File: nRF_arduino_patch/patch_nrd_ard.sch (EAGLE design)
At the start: 14 parts

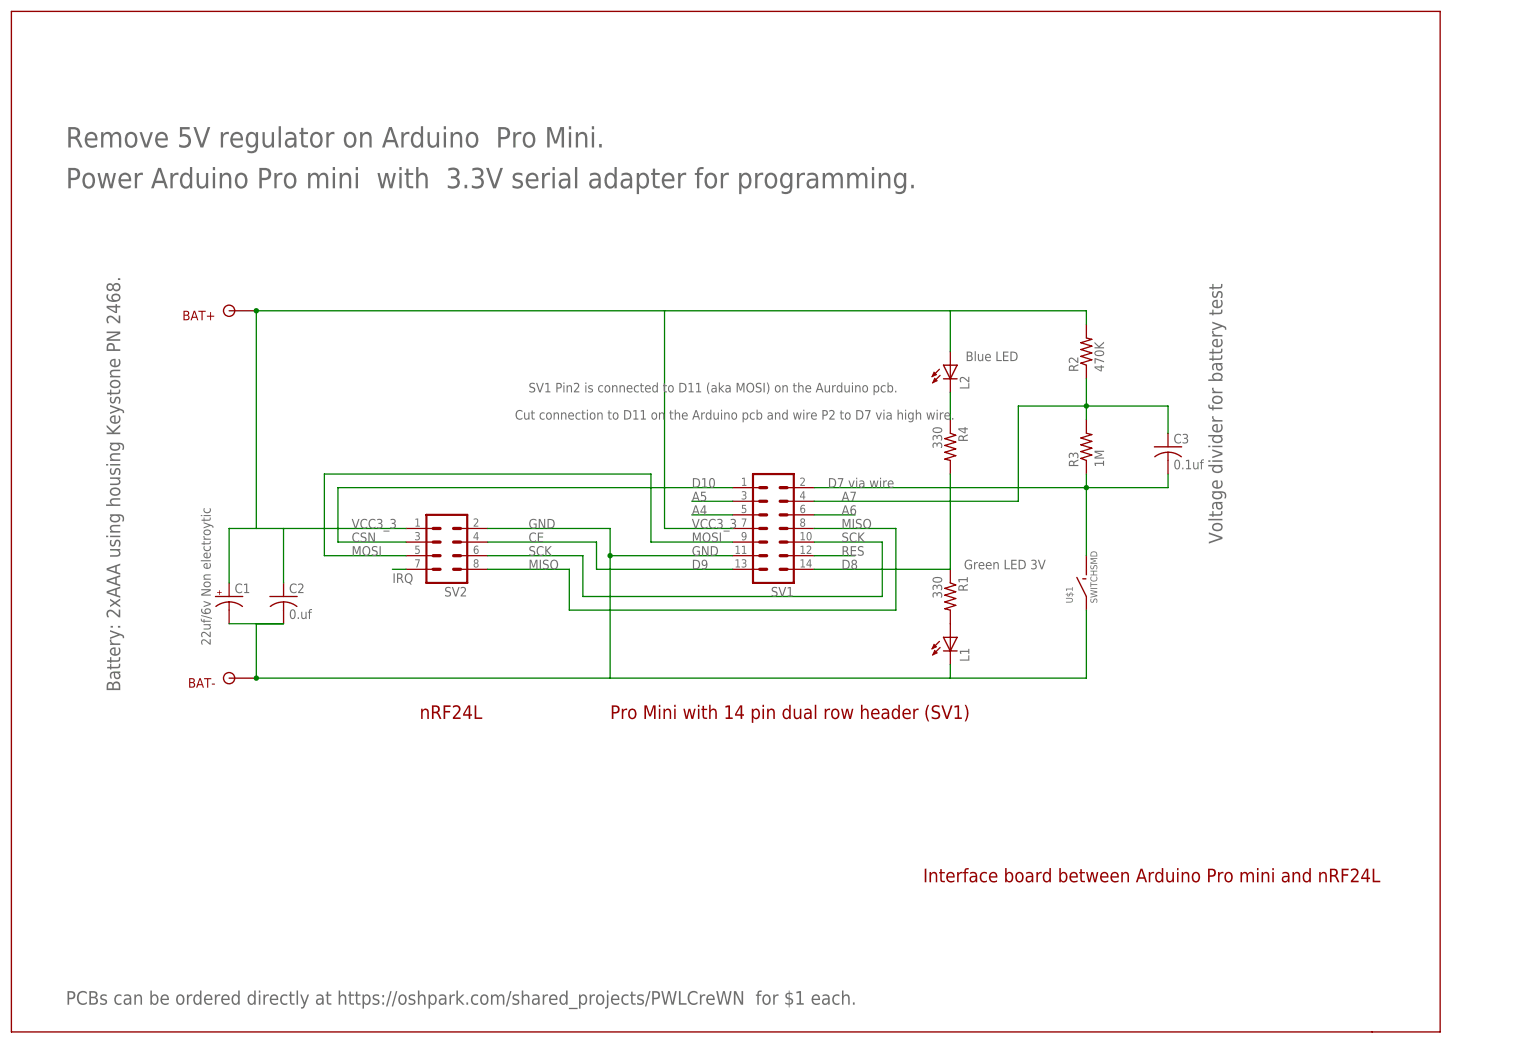
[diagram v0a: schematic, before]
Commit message: added  Nano Modem some modifications on nRFPatch board
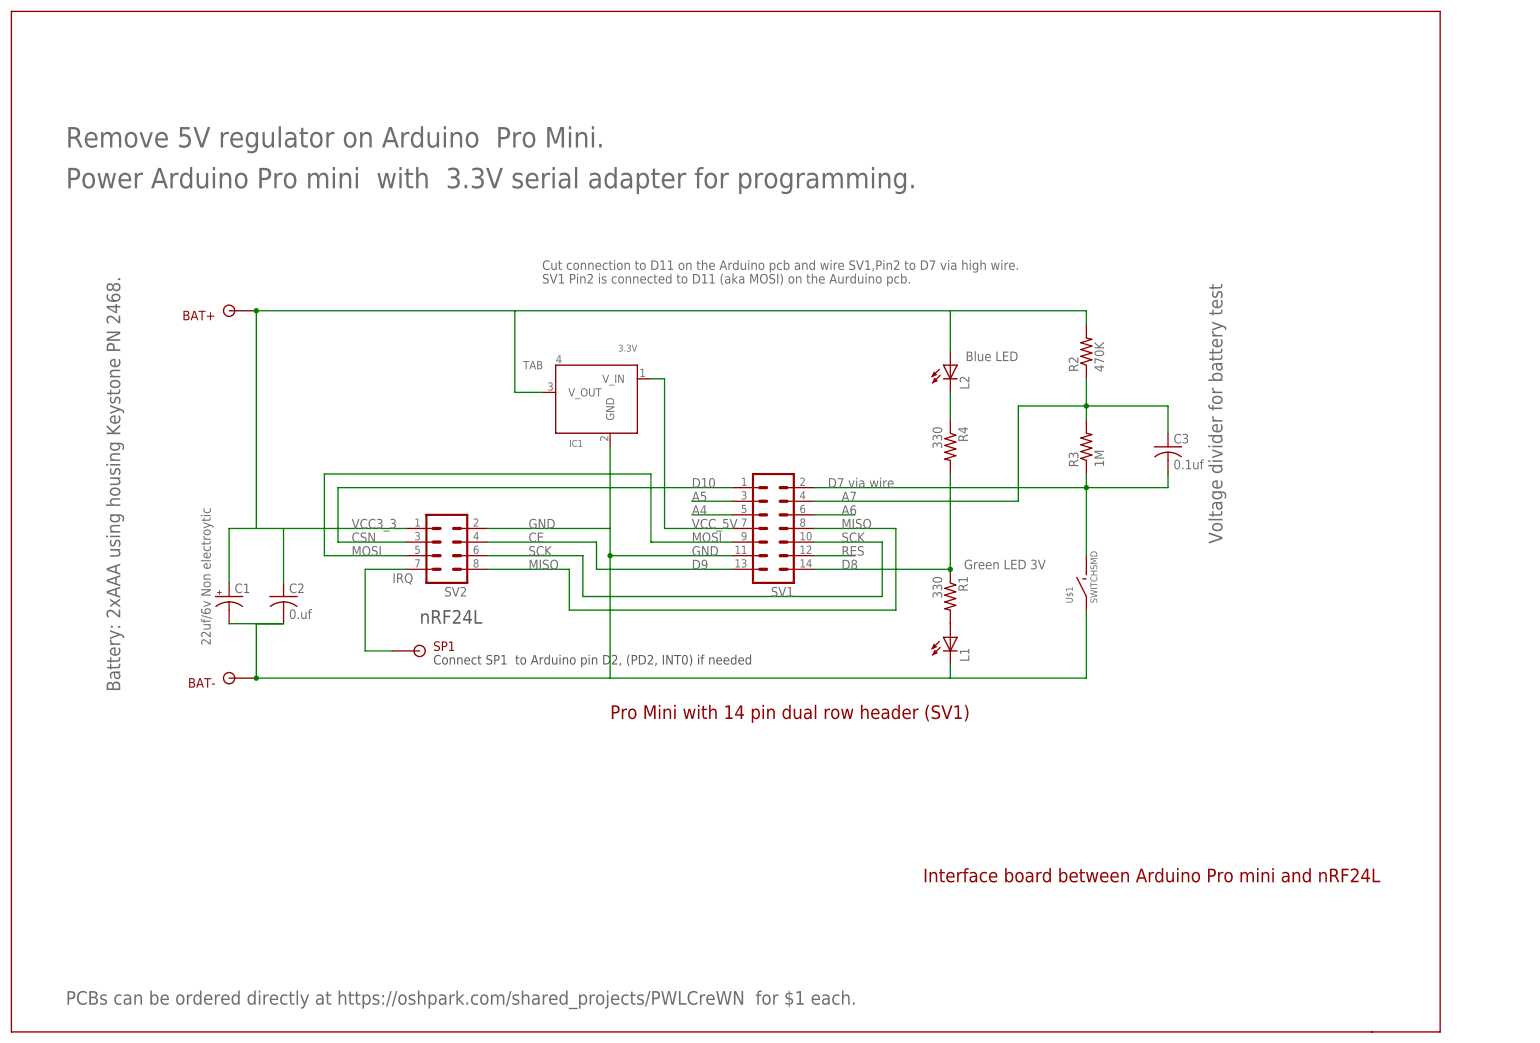
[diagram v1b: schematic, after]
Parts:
- added IC1: 3.3V, 1AA_Stofer:MCP1703ASOT223
- added SP1: SOLDER_POINTA, 1AA_Stofer:SOLDER_POINTA
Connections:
- new net VCC_5V: IC1.V_IN, SV1.7
- net GND: now also IC1.GND
- net IRQ: now also SP1.P$1
- net VCC3_3: now also IC1.V_OUT; no longer SV1.7
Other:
- note added: "Connect SP1 to Arduino pin D2, (PD2, INT0) if needed"
- note added: "Cut connection to D11 on the Arduino pcb and wire SV1,Pin2 to D7 via high wire."
- note removed: "Cut connection to D11 on the Arduino pcb and wire P2 to D7 via high wire."
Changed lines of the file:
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@@
 <layer number="106" name="BGA-Top" color="4" fill="1" visible="yes" active="yes"/>
 <layer number="107" name="BD-Top" color="5" fill="1" visible="yes" active="yes"/>
+<layer number="108" name="centerline" color="7" fill="1" visible="yes" active="yes"/>
 <layer number="116" name="Patch_BOT" color="9" fill="4" visible="yes" active="yes"/>
 <layer number="121" name="_tsilk" color="7" fill="1" visible="yes" active="yes"/>
 <layer number="122" name="_bsilk" color="7" fill="1" visible="yes" active="yes"/>
 <layer number="125" name="_tNames" color="7" fill="1" visible="yes" active="yes"/>
+<layer number="131" name="prix" color="7" fill="1" visible="yes" active="yes"/>
+<layer number="132" name="test" color="7" fill="1" visible="yes" active="yes"/>
 <layer number="144" name="Drill_legend" color="7" fill="1" visible="yes" active="yes"/>
 <layer number="151" name="HeatSink" color="7" fill="1" visible="yes" active="yes"/>
@@
 <part name="C3" library="rcl" deviceset="C-US" device="C0805" value="0.1uf"/>
 <part name="U$2" library="1AA_Stofer" deviceset="8.5X11" device=""/>
+<part name="IC1" library="1AA_Stofer" deviceset="MCP1703A" device="SOT223" value=" 3.3V"/>
+<part name="SP1" library="1AA_Stofer" deviceset="SOLDER_POINT" device="A"/>
 </parts>
 <sheets>
@@
 <text x="172.72" y="-25.4" size="2.54" layer="94">Interface board between Arduino Pro mini and nRF24L</text>
 <text x="114.3" y="5.08" size="2.54" layer="94">Pro Mini with 14 pin dual row header (SV1) </text>
-<text x="78.74" y="5.08" size="2.54" layer="94">nRF24L</text>
+<text x="78.74" y="22.86" size="2.54" layer="97">nRF24L</text>
 <text x="226.06" y="86.36" size="2.54" layer="95" rot="R270">Voltage divider for battery test</text>
 <text x="22.86" y="10.16" size="2.54" layer="95" rot="R90">Battery: 2xAAA using housing Keystone PN 2468. </text>
 <text x="190.5" y="73.66" size="1.778" layer="95" rot="R180">Blue LED </text>
 <text x="180.34" y="33.02" size="1.778" layer="95">Green LED 3V</text>
-<text x="96.52" y="60.96" size="1.778" layer="95">Cut connection to D11 on the Arduino pcb and wire P2 to D7 via high wire.</text>
-<text x="99.06" y="66.04" size="1.778" layer="95">SV1 Pin2 is connected to D11 (aka MOSI) on the Aurduino pcb. </text>
+<text x="101.6" y="88.9" size="1.778" layer="95">Cut connection to D11 on the Arduino pcb and wire SV1,Pin2 to D7 via high wire.</text>
+<text x="101.6" y="86.36" size="1.778" layer="95">SV1 Pin2 is connected to D11 (aka MOSI) on the Aurduino pcb. </text>
 <text x="12.7" y="-48.26" size="2.54" layer="95">PCBs can be ordered directly at https://oshpark.com/shared_projects/PWLCreWN  for $1 each.</text>
 <text x="12.7" y="111.76" size="3.81" layer="95">Remove 5V regulator on Arduino  Pro Mini.</text>
 <text x="12.7" y="104.14" size="3.81" layer="95">Power Arduino Pro mini  with  3.3V serial adapter for programming.</text>
+<text x="81.28" y="15.24" size="1.778" layer="97">Connect SP1  to Arduino pin D2, (PD2, INT0) if needed </text>
 </plain>
 <instances>
@@
 <instance part="U$2" gate="G$1" x="2.54" y="-53.34"/>
 <instance part="U$2" gate="G$2" x="167.64" y="-53.34"/>
+<instance part="IC1" gate="G$1" x="111.76" y="66.04" rot="MR0"/>
+<instance part="SP1" gate="G$1" x="83.82" y="17.78"/>
 </instances>
 <busses>
@@
 <pinref part="R4" gate="G$1" pin="2"/>
 <wire x1="177.8" y1="50.8" x2="177.8" y2="33.02" width="0.1524" layer="91"/>
+<junction x="177.8" y="33.02"/>
 </segment>
 </net>
@@
 <segment>
 <pinref part="SV2" gate="G$1" pin="7"/>
-<wire x1="76.2" y1="33.02" x2="73.66" y2="33.02" width="0.1524" layer="91"/>
 <label x="73.66" y="30.48" size="1.778" layer="95"/>
+<wire x1="76.2" y1="33.02" x2="68.58" y2="33.02" width="0.1524" layer="91"/>
+<wire x1="68.58" y1="33.02" x2="68.58" y2="17.78" width="0.1524" layer="91"/>
+<pinref part="SP1" gate="G$1" pin="P$1"/>
+<wire x1="68.58" y1="17.78" x2="73.66" y2="17.78" width="0.1524" layer="91"/>
 </segment>
 </net>
@@
 <net name="GND" class="0">
 <segment>
-<label x="129.54" y="35.56" size="1.778" layer="95"/>
 <pinref part="SV2" gate="G$1" pin="2"/>
 <label x="99.06" y="40.64" size="1.778" layer="95"/>
 <wire x1="91.44" y1="40.64" x2="114.3" y2="40.64" width="0.1524" layer="91"/>
-<wire x1="114.3" y1="40.64" x2="114.3" y2="35.56" width="0.1524" layer="91"/>
 <pinref part="C1" gate="G$1" pin="-"/>
 <wire x1="53.34" y1="22.86" x2="48.26" y2="22.86" width="0.1524" layer="91"/>
@@
 <pinref part="C2" gate="G$1" pin="2"/>
 <wire x1="43.18" y1="22.86" x2="53.34" y2="22.86" width="0.1524" layer="91"/>
+<wire x1="114.3" y1="40.64" x2="114.3" y2="35.56" width="0.1524" layer="91"/>
+<pinref part="L1" gate="G$1" pin="C"/>
 <wire x1="114.3" y1="35.56" x2="114.3" y2="12.7" width="0.1524" layer="91"/>
-<pinref part="L1" gate="G$1" pin="C"/>
 <wire x1="177.8" y1="15.24" x2="177.8" y2="12.7" width="0.1524" layer="91"/>
 <wire x1="48.26" y1="12.7" x2="114.3" y2="12.7" width="0.1524" layer="91"/>
 <wire x1="114.3" y1="12.7" x2="177.8" y2="12.7" width="0.1524" layer="91"/>
 <wire x1="203.2" y1="12.7" x2="177.8" y2="12.7" width="0.1524" layer="91"/>
-<junction x="114.3" y="35.56"/>
 <pinref part="U$1" gate="G$1" pin="P$2"/>
 <wire x1="203.2" y1="12.7" x2="203.2" y2="25.4" width="0.1524" layer="91"/>
+<pinref part="BAT-" gate="G$1" pin="P$1"/>
+<junction x="48.26" y="12.7"/>
+<pinref part="IC1" gate="G$1" pin="GND"/>
+<wire x1="114.3" y1="40.64" x2="114.3" y2="55.88" width="0.1524" layer="91"/>
 <pinref part="SV1" gate="G$1" pin="11"/>
 <wire x1="137.16" y1="35.56" x2="114.3" y2="35.56" width="0.1524" layer="91"/>
-<pinref part="BAT-" gate="G$1" pin="P$1"/>
-<junction x="48.26" y="12.7"/>
+<label x="129.54" y="35.56" size="1.778" layer="95"/>
+<junction x="114.3" y="35.56"/>
 </segment>
 </net>
@@
 <wire x1="43.18" y1="40.64" x2="48.26" y2="40.64" width="0.1524" layer="91"/>
 <wire x1="48.26" y1="40.64" x2="48.26" y2="81.28" width="0.1524" layer="91"/>
-<pinref part="SV1" gate="G$1" pin="7"/>
-<label x="129.54" y="40.64" size="1.778" layer="95"/>
-<wire x1="137.16" y1="40.64" x2="124.46" y2="40.64" width="0.1524" layer="91"/>
-<wire x1="124.46" y1="40.64" x2="124.46" y2="81.28" width="0.1524" layer="91"/>
-<wire x1="48.26" y1="81.28" x2="124.46" y2="81.28" width="0.1524" layer="91"/>
+<wire x1="48.26" y1="81.28" x2="96.52" y2="81.28" width="0.1524" layer="91"/>
 <pinref part="R2" gate="G$1" pin="2"/>
-<wire x1="124.46" y1="81.28" x2="177.8" y2="81.28" width="0.1524" layer="91"/>
+<wire x1="96.52" y1="81.28" x2="177.8" y2="81.28" width="0.1524" layer="91"/>
 <wire x1="177.8" y1="81.28" x2="203.2" y2="81.28" width="0.1524" layer="91"/>
 <wire x1="203.2" y1="81.28" x2="203.2" y2="78.74" width="0.1524" layer="91"/>
@@
 <pinref part="L2" gate="G$1" pin="A"/>
 <wire x1="177.8" y1="73.66" x2="177.8" y2="81.28" width="0.1524" layer="91"/>
+<pinref part="IC1" gate="G$1" pin="V_OUT"/>
+<wire x1="101.6" y1="66.04" x2="96.52" y2="66.04" width="0.1524" layer="91"/>
+<wire x1="96.52" y1="66.04" x2="96.52" y2="81.28" width="0.1524" layer="91"/>
 </segment>
 </net>
@@
 </segment>
 </net>
+<net name="VCC_5V" class="0">
+<segment>
+<pinref part="SV1" gate="G$1" pin="7"/>
+<wire x1="137.16" y1="40.64" x2="124.46" y2="40.64" width="0.1524" layer="91"/>
+<label x="129.54" y="40.64" size="1.778" layer="95"/>
+<wire x1="124.46" y1="40.64" x2="124.46" y2="68.58" width="0.1524" layer="91"/>
+<pinref part="IC1" gate="G$1" pin="V_IN"/>
+<wire x1="124.46" y1="68.58" x2="121.92" y2="68.58" width="0.1524" layer="91"/>
+</segment>
+</net>
